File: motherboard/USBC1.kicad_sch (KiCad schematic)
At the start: 32 parts, among them J5 USB_C_Receptacle, U1 TPD4EUSB30, U2 TPD4EUSB30, U3 TPD4EUSB30, U4 FUSB302BMPX, U5 SY6280AAC

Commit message: hdmi, edp, peripheral implementations
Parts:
- renumbered C1 to C14, C9 to C15, C10 to C16, C4 to C17, C5 to C18, C12 to C19, C13 to C20, C6 to C21, C7 to C22, C8 to C23, C11 to C24, C3 to C25, C2 to C26, CMC1 to CMC2, D1 to D2, J5 to J6, R8 to R12, R9 to R13, R6 to R14, R7 to R15, R4 to R16, R5 to R17, R11 to R18, R10 to R19, R1 to R20, R2 to R21, R3 to R22, U2 to U10, U5 to U6, U4 to U7, U3 to U8, U1 to U9

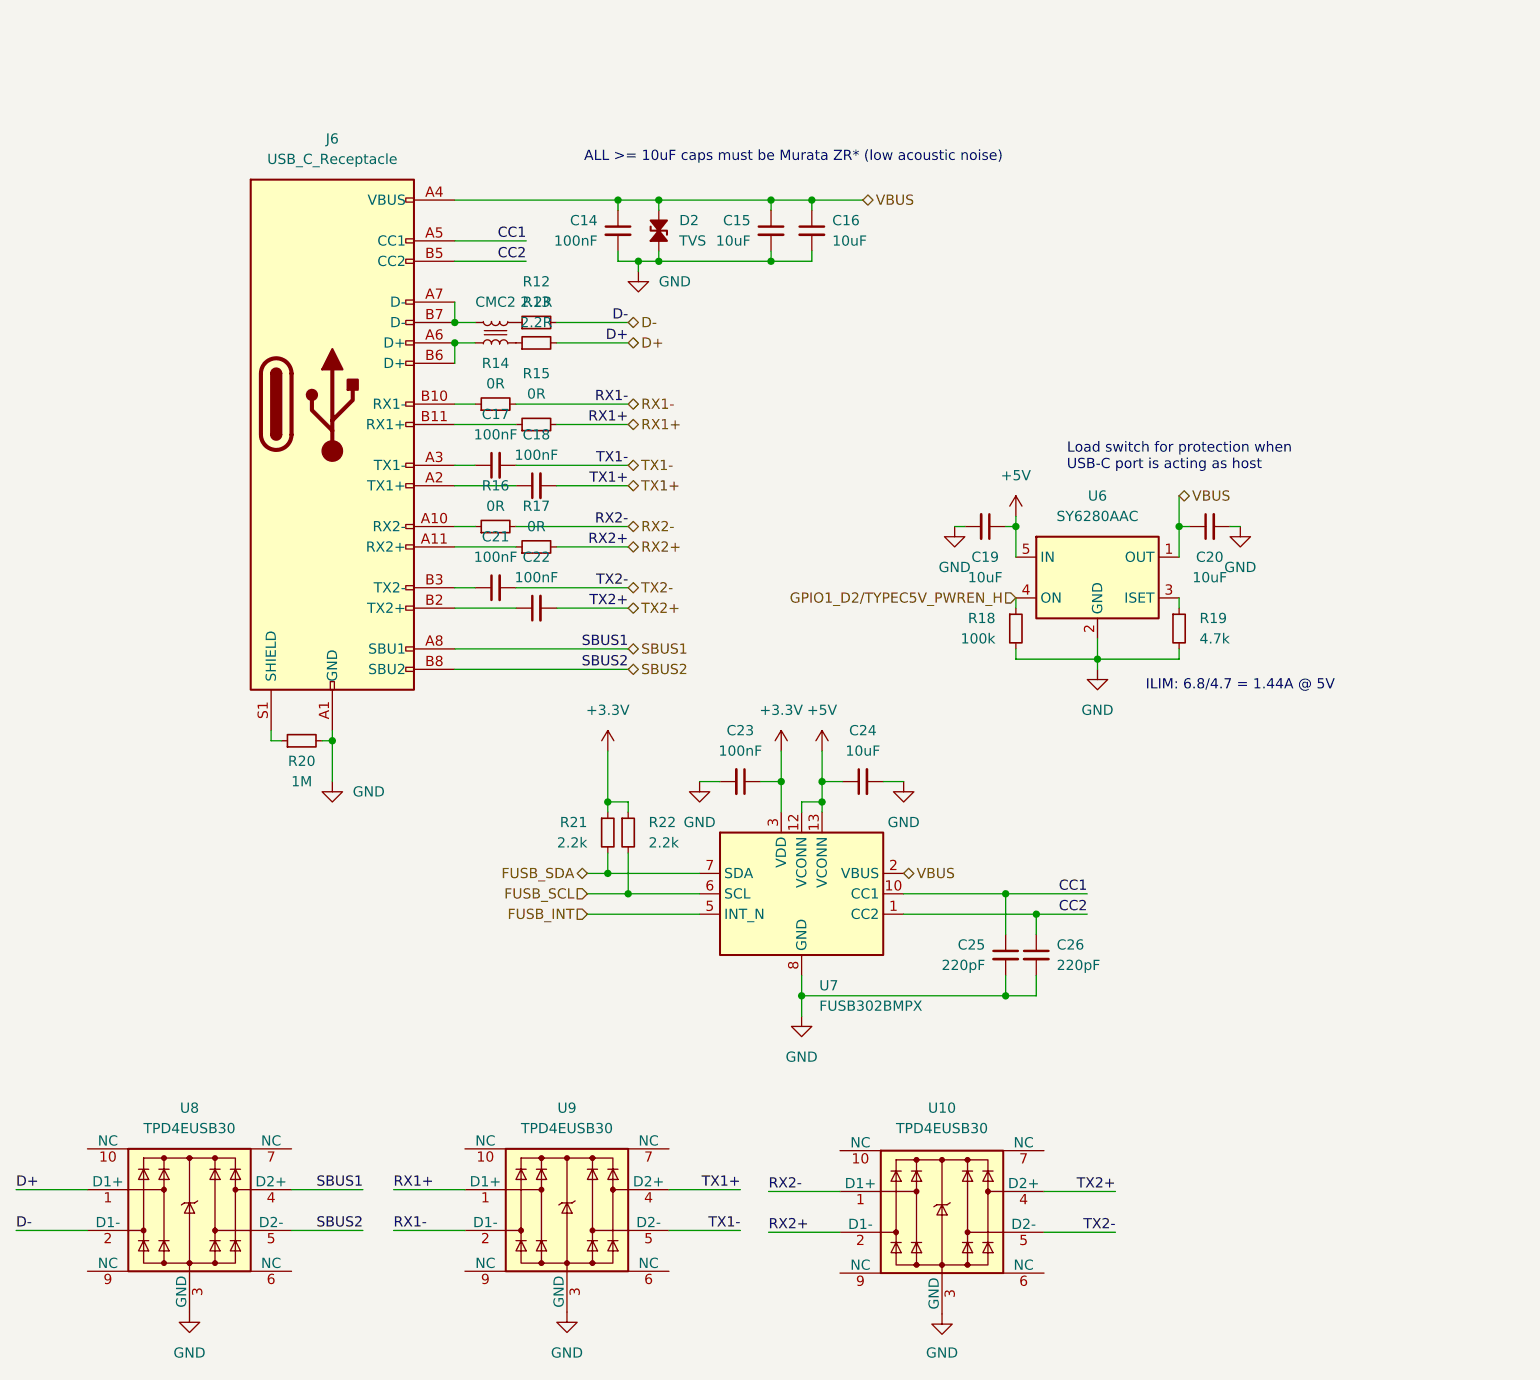
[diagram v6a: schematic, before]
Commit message: synchronizing hierarchical pins
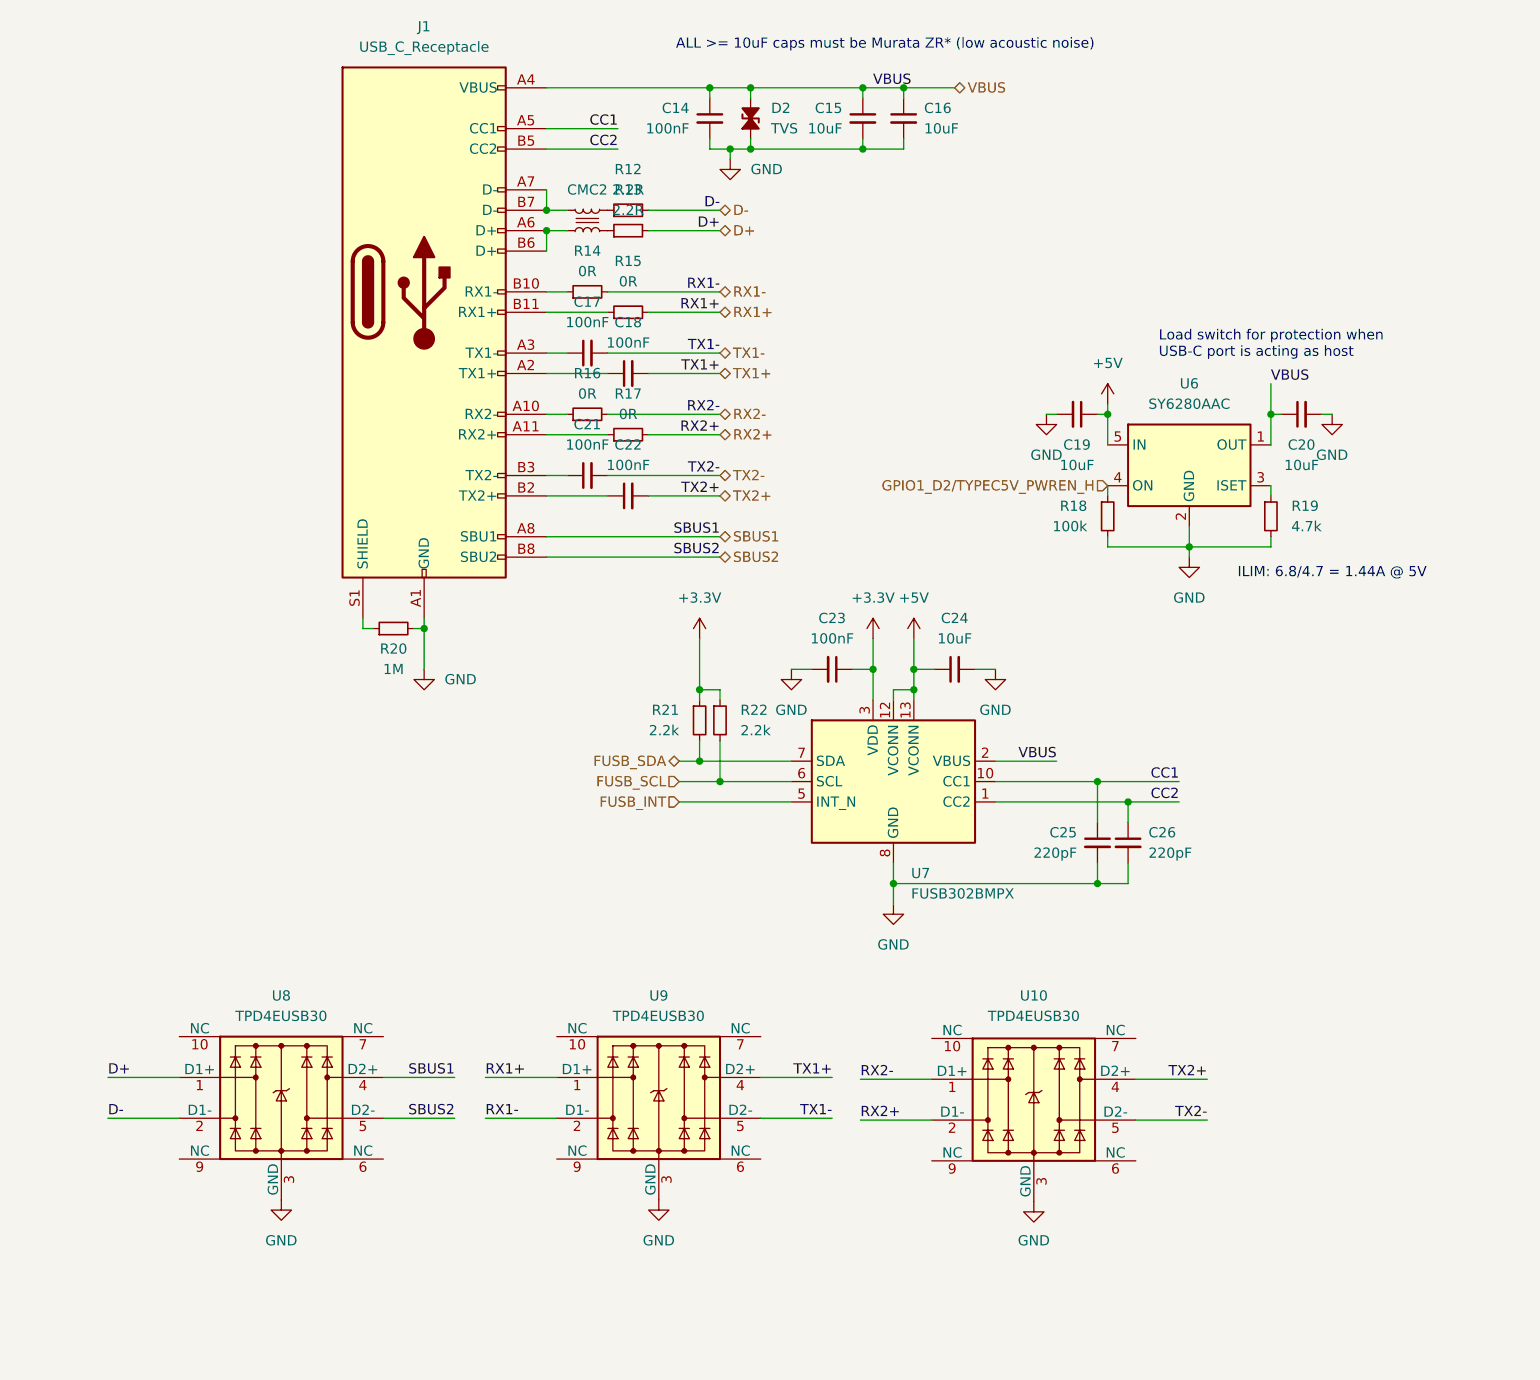
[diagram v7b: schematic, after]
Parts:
- removed J6: USB_C_Receptacle, symbol Connector:USB_C_Receptacle
- added J1: USB_C_Receptacle, symbol Connector:USB_C_Receptacle
- C14, C15, C16, C17, C18, C19, C20, C21, C22, C23, C24, C25, C26: footprint (none) -> Capacitor_SMD:C_0402_1005Metric
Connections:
- net CC1: now also J1.A5 (CC1)
- net CC2: now also J1.B5 (CC2)
- net GND: now also J1.A1 (GND), J1.A12 (GND), J1.B1 (GND), J1.B12 (GND)
- net SBUS1: now also J1.A8 (SBU1)
- net SBUS2: now also J1.B8 (SBU2)
- net VBUS: now also J1.A4 (VBUS), J1.A9 (VBUS), J1.B4 (VBUS), J1.B9 (VBUS)
- net at C22.1: now also J1.B2 (TX2+)
- net at R17.1: now also J1.A11 (RX2+)
- net at C17.1: now also J1.A3 (TX1-)
- net at R15.1: now also J1.B11 (RX1+)
- net at R16.1: now also J1.A10 (RX2-)
- net at R14.1: now also J1.B10 (RX1-)
- net at R20.1: now also J1.S1 (SHIELD)
- net at C21.1: now also J1.B3 (TX2-)
- net at C18.1: now also J1.A2 (TX1+)
- net at CMC2.2: now also J1.A6 (D+), J1.B6 (D+)
- net at CMC2.1: now also J1.A7 (D-), J1.B7 (D-)

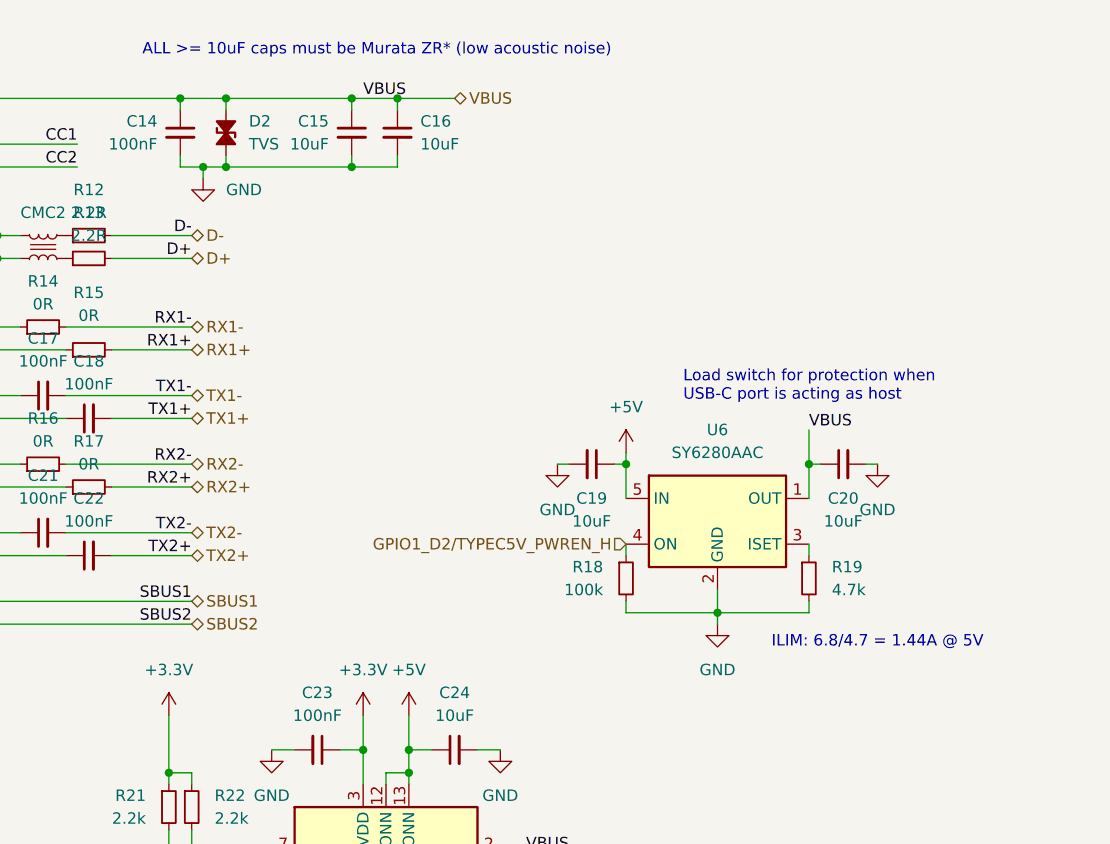
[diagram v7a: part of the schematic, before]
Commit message: linked all footprints
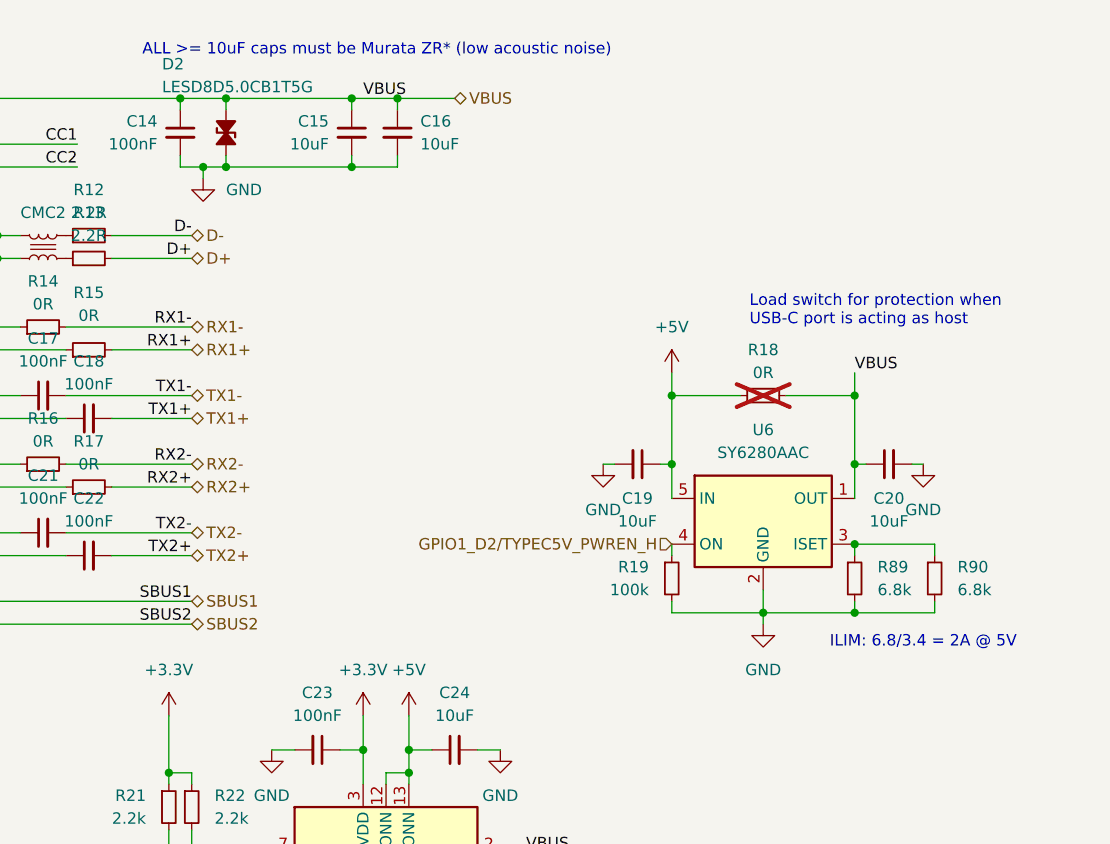
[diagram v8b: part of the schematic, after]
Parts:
- added R89, R90: 6.8k, Resistor_SMD:R_0402_1005Metric, symbol Device:R_Small
- D2: value TVS -> LESD8D5.0CB1T5G; footprint (none) -> Diode_SMD:D_SOD-882
- J1: footprint (none) -> USB-C:USB-C-SMD_TYPE-C-24P-QT
- R12, R13, R14, R15, R16, R17, R20, R21, R22: footprint (none) -> Resistor_SMD:R_0402_1005Metric
- R18: value 100k -> 0R; footprint (none) -> Resistor_SMD:R_0402_1005Metric; now not fitted
- R19: value 4.7k -> 100k; footprint (none) -> Resistor_SMD:R_0402_1005Metric
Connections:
- net +5V: now also R18.1
- net GND: now also R89.2, R90.2; no longer R18.2
- net GPIO1_D2/TYPEC5V_PWREN_H: now also R19.1; no longer R18.1
- net VBUS: now also R18.2
- net at U6.3 (ISET): now also R89.1, R90.1; no longer R19.1
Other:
- note added: "ILIM: 6.8/3.4 = 2A @ 5V"
- note removed: "ILIM: 6.8/4.7 = 1.44A @ 5V"
